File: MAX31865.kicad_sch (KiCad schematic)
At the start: 22 parts, among them J1 Screw_Terminal_01x04, J2 connector, U1 MAX31865, U2 MIC5225

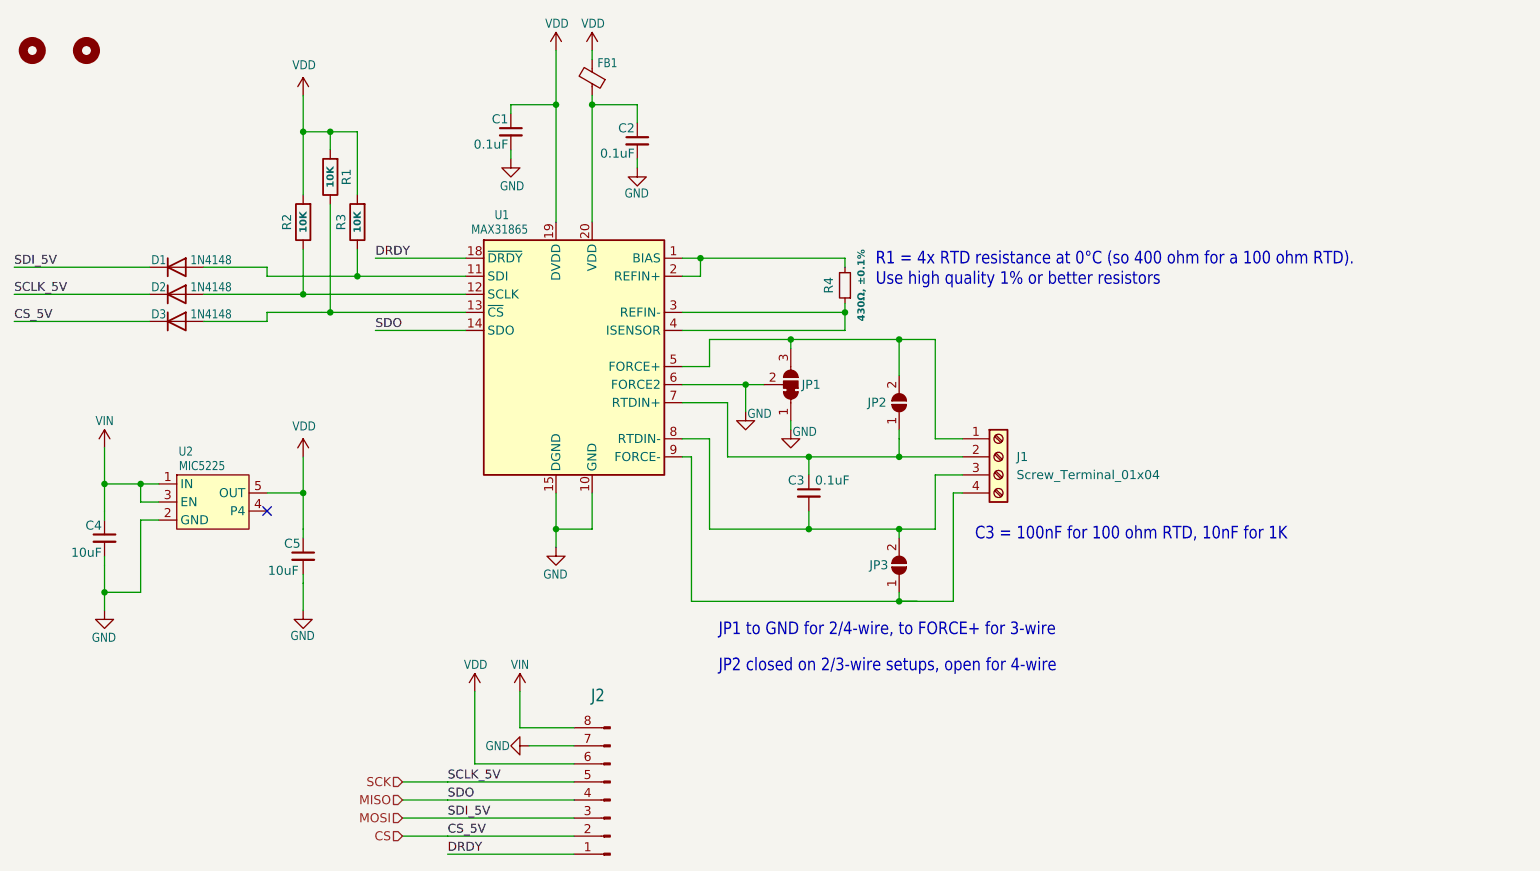
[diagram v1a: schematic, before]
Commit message: added pyrano, anemo, AM2315C, power supply, LEDs, switch and FPC connector in schematic
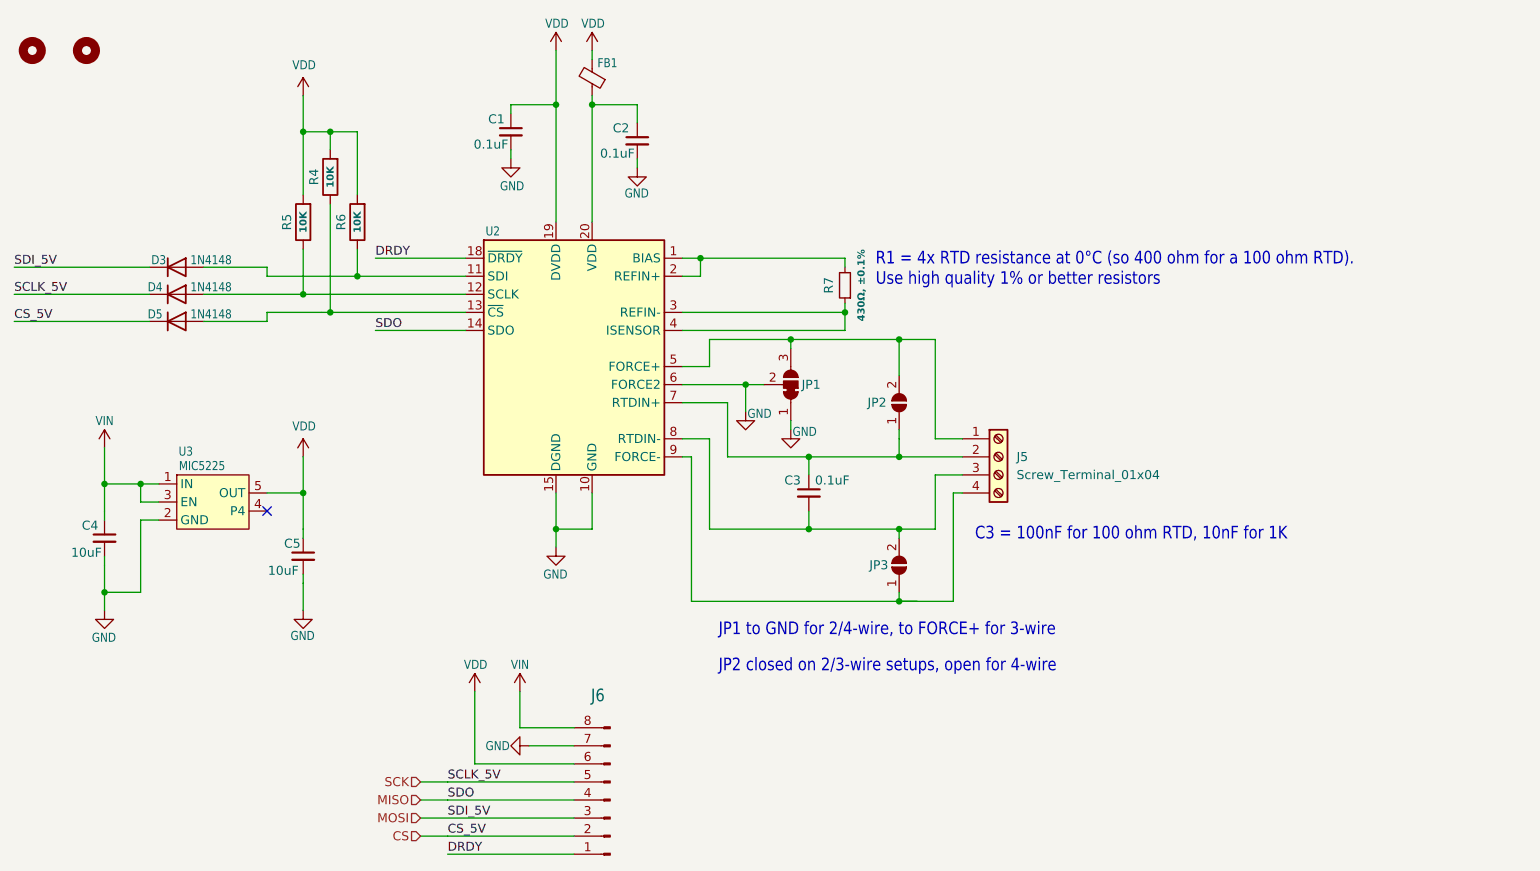
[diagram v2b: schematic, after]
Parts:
- renumbered D1 to D3, D2 to D4, D3 to D5, J1 to J5, J2 to J6, R1 to R4, R2 to R5, R3 to R6, R4 to R7, U1 to U2, U2 to U3

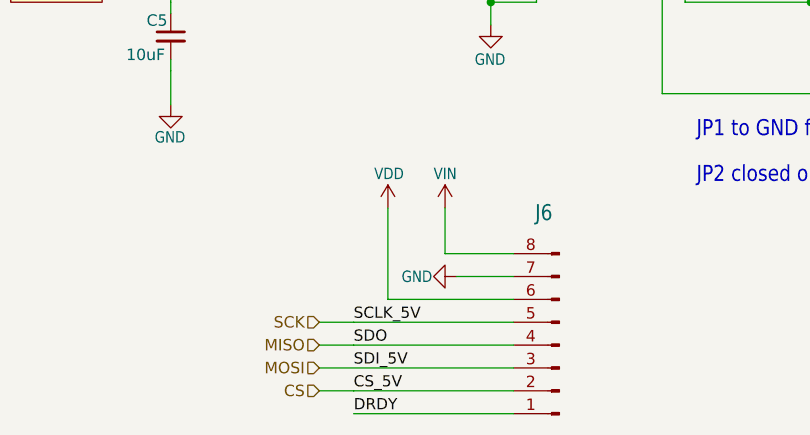
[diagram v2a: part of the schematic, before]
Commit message: removed connectors from modules
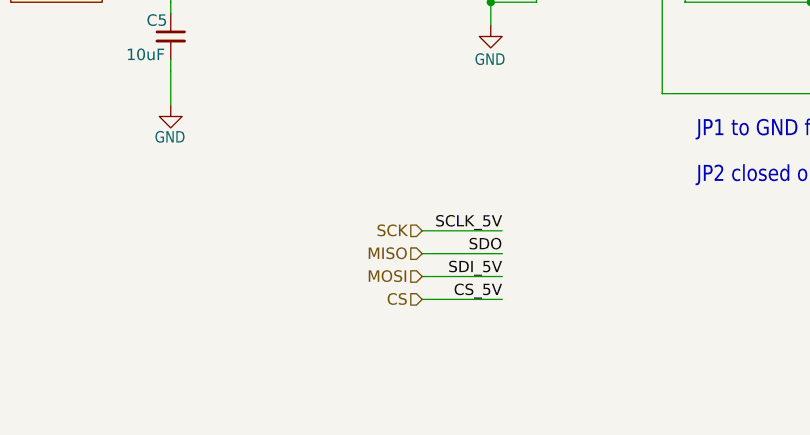
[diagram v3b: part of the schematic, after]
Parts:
- removed J6: connector, Connector_PinHeader_2.54mm:PinHeader_1x08_P2.54mm_Vertical, symbol Connector:Conn_01x08_Pin

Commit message: added MAX31865 external files
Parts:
- U3: symbol external_library:MIC5225 -> MAX31865:MIC5225
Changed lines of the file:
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@@
 	)
 	(symbol
-		(lib_id "external_library:MIC5225")
+		(lib_id "MAX31865:MIC5225")
 		(at 81.28 105.41 0)
 		(unit 1)

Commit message: restructuring of external files
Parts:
- U3: symbol MAX31865:MIC5225 -> external_symbols:MIC5225
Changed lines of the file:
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@@
 	)
 	(symbol
-		(lib_id "MAX31865:MIC5225")
+		(lib_id "external_symbols:MIC5225")
 		(at 81.28 105.41 0)
 		(unit 1)

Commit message: added PCB layout
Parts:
- J5: value Screw_Terminal_01x04 -> Pt100
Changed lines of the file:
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@@
 			)
 		)
-		(property "Value" "Screw_Terminal_01x04"
+		(property "Value" "Pt100"
 			(at 199.39 97.7899 0)
 			(effects

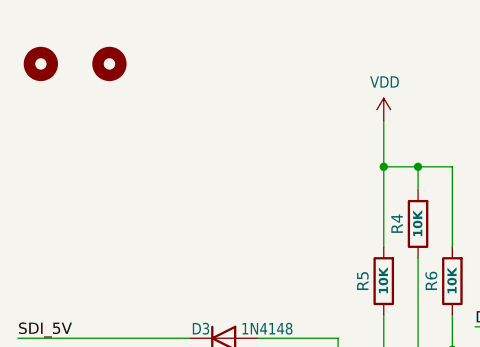
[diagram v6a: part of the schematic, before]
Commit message: removed mouting holes
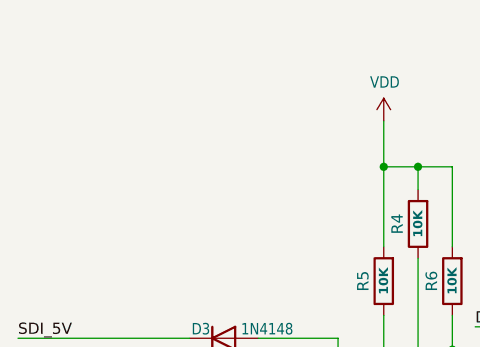
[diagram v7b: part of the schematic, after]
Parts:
- removed U$1, U$2: MOUNTINGHOLE2.5, MountingHole:MountingHole_2.2mm_M2_ISO7380, symbol Mechanical:MountingHole
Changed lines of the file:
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@@
-	)
-	(symbol
-		(lib_id "Mechanical:MountingHole")
-		(at 60.96 38.1 0)
-		(unit 1)
-		(exclude_from_sim yes)
-		(in_bom no)
-		(on_board yes)
-		(dnp no)
-		(property "Reference" "U$1"
-			(at 60.96 38.1 0)
-			(effects
-				(font
-					(size 1.27 1.27)
-				)
-				(hide yes)
-			)
-		)
-		(property "Value" "MOUNTINGHOLE2.5"
-			(at 60.96 38.1 0)
-			(effects
-				(font
-					(size 1.27 1.27)
-				)
-				(hide yes)
-			)
-		)
-		(property "Footprint" "MountingHole:MountingHole_2.2mm_M2_ISO7380"
-			(at 60.96 38.1 0)
-			(effects
-				(font
-					(size 1.27 1.27)
-				)
-				(hide yes)
-			)
-		)
-		(property "Datasheet" "~"
-			(at 60.96 38.1 0)
-			(effects
-				(font
-					(size 1.27 1.27)
-				)
-				(hide yes)
-			)
-		)
-		(property "Description" "Mounting Hole without connection"
-			(at 60.96 38.1 0)
-			(effects
-				(font
-					(size 1.27 1.27)
-				)
-				(hide yes)
-			)
-		)
-		(property "Component package type" ""
-			(at 60.96 38.1 0)
-			(effects
-				(font
-					(size 1.27 1.27)
-				)
-				(hide yes)
-			)
-		)
-		(property "MPN" ""
-			(at 60.96 38.1 0)
-			(effects
-				(font
-					(size 1.27 1.27)
-				)
-				(hide yes)
-			)
-		)
-		(property "Manufacturer" ""
-			(at 60.96 38.1 0)
-			(effects
-				(font
-					(size 1.27 1.27)
-				)
-				(hide yes)
-			)
-		)
-		(property "SPN" ""
-			(at 60.96 38.1 0)
-			(effects
-				(font
-					(size 1.27 1.27)
-				)
-				(hide yes)
-			)
-		)
-		(property "Supplier" ""
-			(at 60.96 38.1 0)
-			(effects
-				(font
-					(size 1.27 1.27)
-				)
-				(hide yes)
-			)
-		)
-		(instances
-			(project "testing-station"
-				(path "/ed3950ec-e24f-4dd6-b9cc-eca012f1333b/d3c2899f-e06d-436a-b13e-f951511bf9c5"
-					(reference "U$1")
-					(unit 1)
-				)
-				(path "/ed3950ec-e24f-4dd6-b9cc-eca012f1333b/e646e214-cec3-4f14-b9f0-d7bac185d28f"
-					(reference "U$3")
-					(unit 1)
-				)
-				(path "/ed3950ec-e24f-4dd6-b9cc-eca012f1333b/555649cf-4903-46cd-aa63-9d48293bec40"
-					(reference "U$5")
-					(unit 1)
-				)
-			)
-		)
 	)
 	(symbol
@@
 					(unit 1)
 				)
-			)
-		)
-	)
-	(symbol
-		(lib_id "Mechanical:MountingHole")
-		(at 68.58 38.1 0)
-		(unit 1)
-		(exclude_from_sim yes)
-		(in_bom no)
-		(on_board yes)
-		(dnp no)
-		(property "Reference" "U$2"
-			(at 68.58 38.1 0)
-			(effects
-				(font
-					(size 1.27 1.27)
-				)
-				(hide yes)
-			)
-		)
-		(property "Value" "MOUNTINGHOLE2.5"
-			(at 68.58 38.1 0)
-			(effects
-				(font
-					(size 1.27 1.27)
-				)
-				(hide yes)
-			)
-		)
-		(property "Footprint" "MountingHole:MountingHole_2.2mm_M2_ISO7380"
-			(at 68.58 38.1 0)
-			(effects
-				(font
-					(size 1.27 1.27)
-				)
-				(hide yes)
-			)
-		)
-		(property "Datasheet" "~"
-			(at 68.58 38.1 0)
-			(effects
-				(font
-					(size 1.27 1.27)
-				)
-				(hide yes)
-			)
-		)
-		(property "Description" "Mounting Hole without connection"
-			(at 68.58 38.1 0)
-			(effects
-				(font
-					(size 1.27 1.27)
-				)
-				(hide yes)
-			)
-		)
-		(property "Component package type" ""
-			(at 68.58 38.1 0)
-			(effects
-				(font
-					(size 1.27 1.27)
-				)
-				(hide yes)
-			)
-		)
-		(property "MPN" ""
-			(at 68.58 38.1 0)
-			(effects
-				(font
-					(size 1.27 1.27)
-				)
-				(hide yes)
-			)
-		)
-		(property "Manufacturer" ""
-			(at 68.58 38.1 0)
-			(effects
-				(font
-					(size 1.27 1.27)
-				)
-				(hide yes)
-			)
-		)
-		(property "SPN" ""
-			(at 68.58 38.1 0)
-			(effects
-				(font
-					(size 1.27 1.27)
-				)
-				(hide yes)
-			)
-		)
-		(property "Supplier" ""
-			(at 68.58 38.1 0)
-			(effects
-				(font
-					(size 1.27 1.27)
-				)
-				(hide yes)
-			)
-		)
-		(instances
-			(project "testing-station"
-				(path "/ed3950ec-e24f-4dd6-b9cc-eca012f1333b/d3c2899f-e06d-436a-b13e-f951511bf9c5"
-					(reference "U$2")
-					(unit 1)
-				)
-				(path "/ed3950ec-e24f-4dd6-b9cc-eca012f1333b/e646e214-cec3-4f14-b9f0-d7bac185d28f"
-					(reference "U$4")
-					(unit 1)
-				)
-				(path "/ed3950ec-e24f-4dd6-b9cc-eca012f1333b/555649cf-4903-46cd-aa63-9d48293bec40"
-					(reference "U$6")
-					(unit 1)
-				)

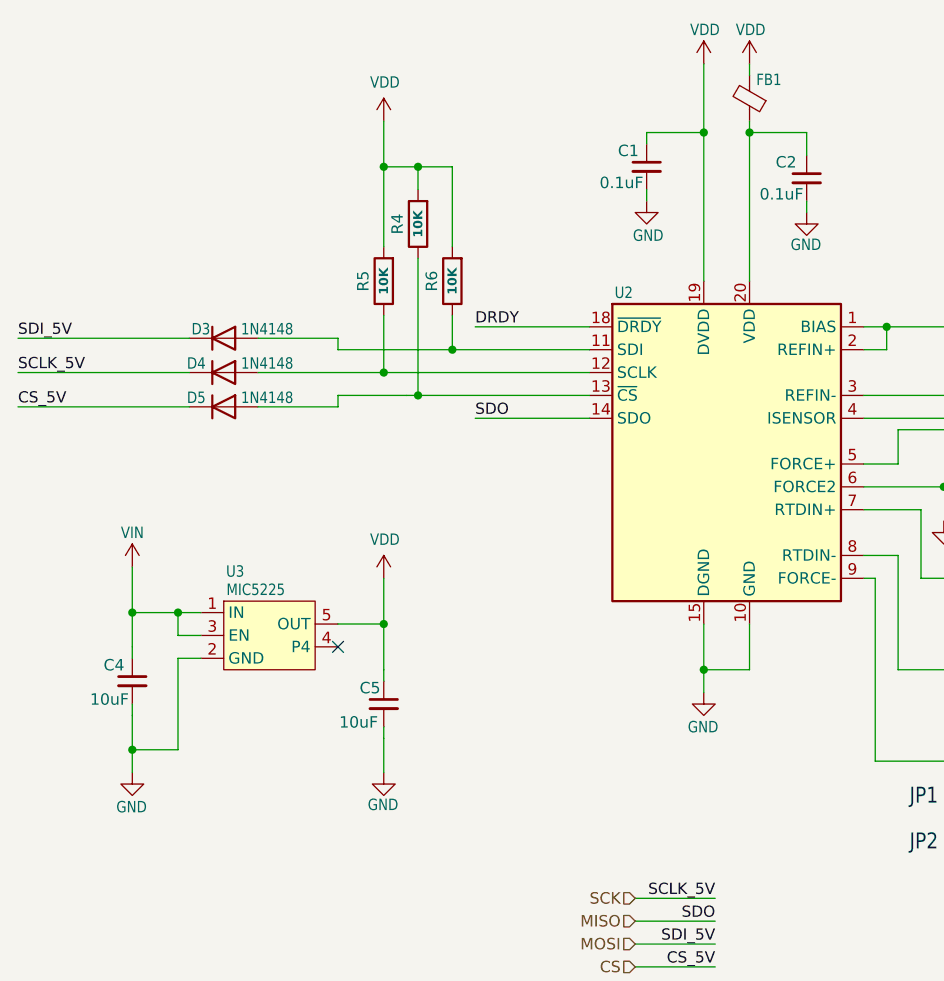
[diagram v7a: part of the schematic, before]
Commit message: removed voltage regulators of each individual module
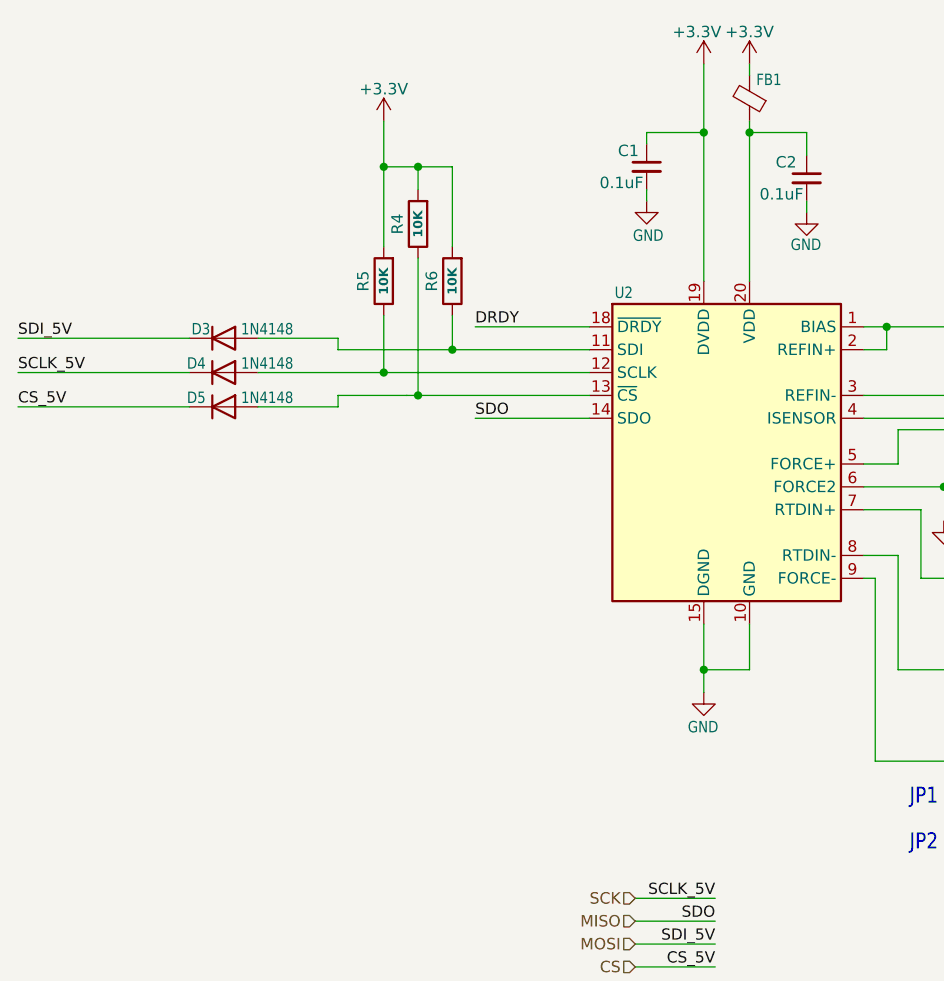
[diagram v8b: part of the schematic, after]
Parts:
- removed C4, C5: 10uF, Capacitor_SMD:C_0805_2012Metric, symbol Device:C_Small
- removed U3: MIC5225, Package_TO_SOT_SMD:SOT-23-5, symbol external_symbols:MIC5225
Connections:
- net VDD renamed +3.3V
- no-connect marks 1 -> 0
